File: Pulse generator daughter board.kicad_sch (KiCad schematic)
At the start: 27 parts, among them J1 PWM1 input, J2 PWM2 input, J3 Vin1, J4 Vin1_GND, J5 Vin2, J6 Vin2_GND, U1 TC4427, U2 TC4427

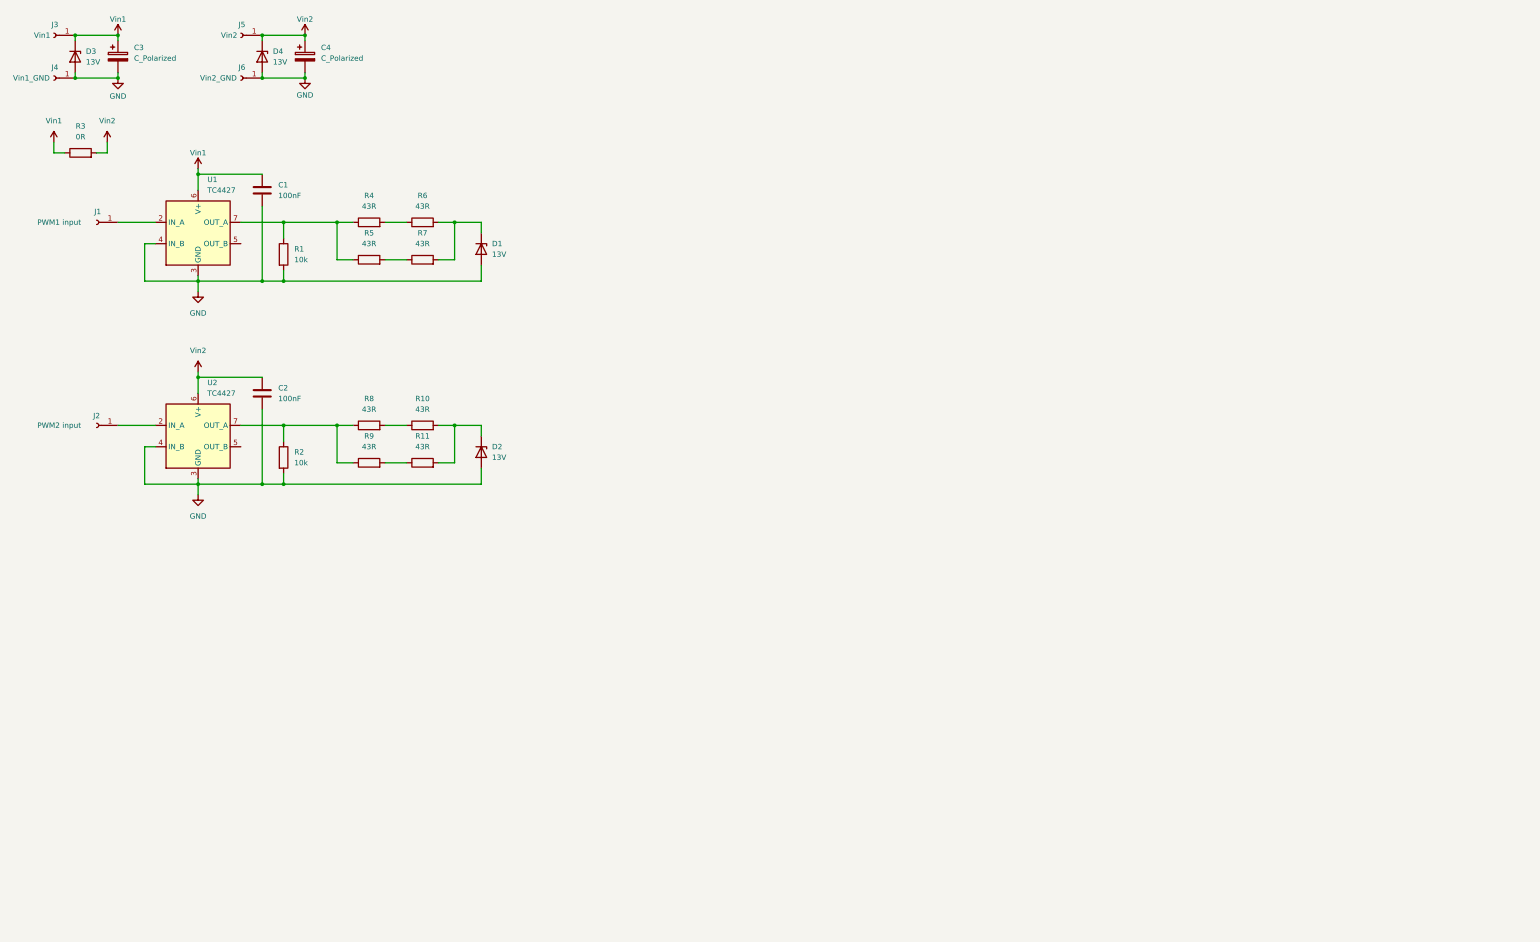
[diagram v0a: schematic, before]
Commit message: PWMs and DWMs done
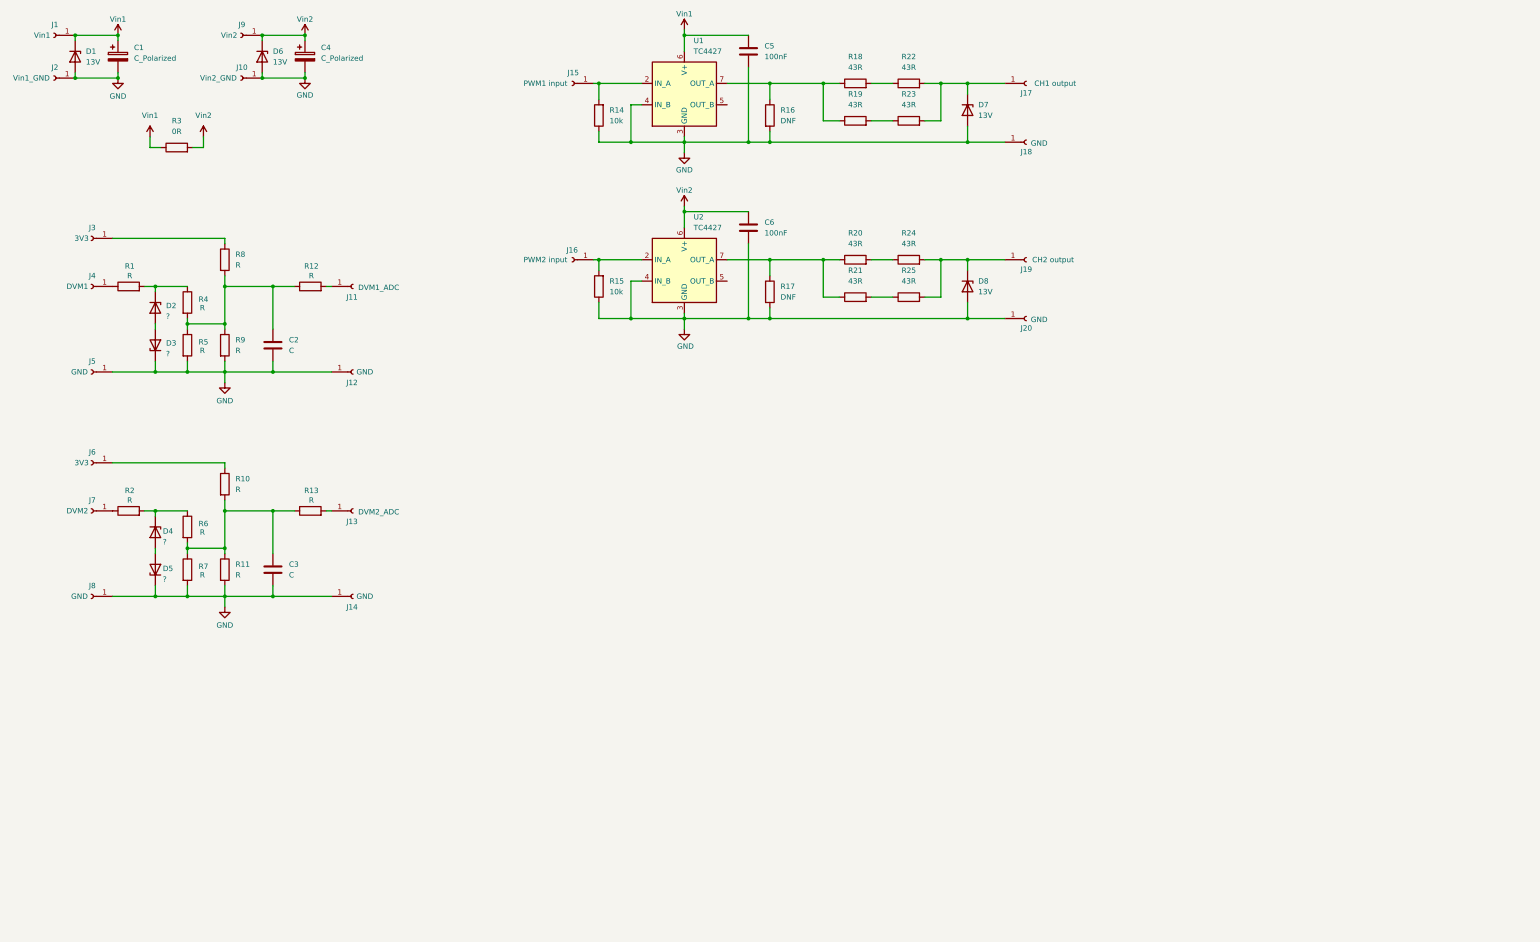
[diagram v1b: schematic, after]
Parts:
- added C2, C3: C, symbol Device:C
- added D2, D3, D4, D5: ?, symbol Device:D_Zener
- added J11: DVM1_ADC, symbol Connector:Conn_01x01_Socket
- added J12, J14, J18, J20, J5, J8: GND, symbol Connector:Conn_01x01_Socket
- added J13: DVM2_ADC, symbol Connector:Conn_01x01_Socket
- added J17: CH1 output, symbol Connector:Conn_01x01_Socket
- added J19: CH2 output, symbol Connector:Conn_01x01_Socket
- added J3, J6: 3V3, symbol Connector:Conn_01x01_Socket
- added J4: DVM1, symbol Connector:Conn_01x01_Socket
- added J7: DVM2, symbol Connector:Conn_01x01_Socket
- added R1, R10, R11, R12, R13, R2, R4, R5, R6, R7, R8, R9: R, symbol Device:R
- added R14, R15: 10k, symbol Device:R
- R16: renamed from R1; value 10k -> DNF
- R17: renamed from R2; value 10k -> DNF
- renumbered C3 to C1, C1 to C5, C2 to C6, D3 to D1, D4 to D6, D1 to D7, D2 to D8, J3 to J1, J6 to J10, J1 to J15, J2 to J16, J4 to J2, J5 to J9, R4 to R18, R5 to R19, R8 to R20, R9 to R21, R6 to R22, R7 to R23, R10 to R24, R11 to R25
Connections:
- net GND: now also C2.2, C3.2, D3.1 (K), D5.1 (K), J12.1 (Pin_1), J14.1 (Pin_1), J18.1 (Pin_1), J20.1 (Pin_1), J5.1 (Pin_1), J8.1 (Pin_1), R11.2, R14.1, R15.1, R5.2, R7.2, R9.2
- net at J15.1 (Pin_1), U1.2 (IN_A): now also R14.2
- net at D7.1 (K), R22.2, R23.2: now also J17.1 (Pin_1)
- net at D8.1 (K), R24.2, R25.2: now also J19.1 (Pin_1)
- net at J16.1 (Pin_1), U2.2 (IN_A): now also R15.2
- new net: D2.1 (K), R1.2, R4.1
- new net: D2.2 (A), D3.2 (A)
- new net: J6.1 (Pin_1), R10.1
- new net: J13.1 (Pin_1), R13.2
- new net: C3.1, R10.2, R11.1, R13.1, R6.2, R7.1
- new net: J3.1 (Pin_1), R8.1
- new net: C2.1, R12.1, R4.2, R5.1, R8.2, R9.1
- new net: J4.1 (Pin_1), R1.1
- new net: J7.1 (Pin_1), R2.1
- new net: J11.1 (Pin_1), R12.2
- new net: D4.1 (K), R2.2, R6.1
- new net: D4.2 (A), D5.2 (A)
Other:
- moved on the sheet: C5, C6, D7, D8, J15, J16, R16, R17, R18, R19, R20, R21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

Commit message: Progress 2 on schematic and PCB
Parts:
- removed J11: DVM1_ADC, symbol Connector:Conn_01x01_Socket
- removed J13: DVM2_ADC, symbol Connector:Conn_01x01_Socket
- removed J15: PWM1 input, symbol Connector:Conn_01x01_Socket
- removed J16: PWM2 input, symbol Connector:Conn_01x01_Socket
- added C1: 10nF, symbol Device:C
- added C4, C5, C9: C, symbol Device:C
- added C6: 100nF, symbol Device:C
- added J15: CN8, Connector_PinHeader_2.54mm:PinHeader_2x08_P2.54mm_Vertical, symbol Connector_Generic:Conn_02x08_Odd_Even
- added J16: CN9, Connector_PinHeader_2.54mm:PinHeader_2x15_P2.54mm_Vertical, symbol Connector_Generic:Conn_02x15_Odd_Even
- added J17: CN7, Connector_PinHeader_2.54mm:PinHeader_2x10_P2.54mm_Vertical, symbol Connector_Generic:Conn_02x10_Odd_Even
- added J18: CN10, Connector_PinHeader_2.54mm:PinHeader_2x17_P2.54mm_Vertical, symbol Connector_Generic:Conn_02x17_Odd_Even
- added U1: MAX31855KASA, Package_SO:SOIC-8_3.9x4.9mm_P1.27mm, symbol Sensor_Temperature:MAX31855KASA
- added U2: ADUM1402, Package_SO:SOIC-16W_7.5x10.3mm_P1.27mm, symbol Rafal_Library:ADUM1402
- C3: value C -> 100nF
- D1, D6, D7, D8: footprint (none) -> Diode_SMD:D_SMA_Handsoldering
- J12: value GND -> T-
- J14: value GND -> T+
- J7: value DVM2 -> DVM1
- R10, R11, R12, R13, R14, R15, R16, R17, R3, R4, R5, R6, R7, R8, R9: footprint (none) -> Resistor_SMD:R_0805_2012Metric_Pad1.20x1.40mm_HandSolder
- R18, R19, R20, R21, R22, R23, R24, R25: footprint (none) -> Resistor_SMD:R_2512_6332Metric_Pad1.40x3.35mm_HandSolder
- renumbered C5 to C10, C6 to C11, C1 to C2, C4 to C7, C2 to C8, J17 to J21, J18 to J22, J19 to J23, J20 to J24, U1 to U3, U2 to U4
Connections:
- net GND: now also R16.1, R17.1, C4.2, C5.2, C9.2, U2. (We2); no longer C3.2, J12.1 (Pin_1), J14.1 (Pin_1), R11.2, R16.2, R17.2, R9.2
- net Vin1: now also D6.1 (K); no longer D1.1 (K)
- net Vin2: now also D8.1 (K); no longer D6.1 (K)
- net at J6.1 (Pin_1), R10.1: now also C5.1
- net PWM1 _CH1: now reaches R14.2, U3.2 (IN_A)
- net PWM1 _CH1: now also J17.10 (Pin_10)
- net ADC2: now reaches R13.2
- net ADC2: now also C9.1, J16.19 (Pin_19)
- net at R10.2, R11.1, R13.1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: no longer C3.1
- net at D7.1 (K), J21.1 (Pin_1): now also R19.2, R21.2; no longer R22.2, R23.2
- net at R25.1: now also R23.2; no longer R21.2
- net at J23.1 (Pin_1), R24.2, R25.2: now also D1.1 (K); no longer D8.1 (K)
- net PWM1 _CH2: now reaches R15.2, U4.2 (IN_A)
- net PWM1 _CH2: now also J18.29 (Pin_29)
- net at R18.1, U3.7 (OUT_A): now also R16.2, R20.1; no longer R16.1, R19.1
- net at J3.1 (Pin_1), R8.1: now also C4.1
- net at R12.1, R4.2, R5.1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: no longer C8.1
- net at R18.2: now also R19.1; no longer R22.1
- net at R24.1: now also R22.2; no longer R20.2
- net at R23.1: now also R17.2, R22.1, U4.7 (OUT_A); no longer R19.2
- net ADC1: now reaches R12.2
- net ADC1: now also C8.1, J16.3 (Pin_3)
- new net: J17.15 (Pin_15), U2. (We2)
- new net: J17.19 (Pin_19), U2. (We2)
- new net: J17.2 (Pin_2), U2. (We2)
- new net: C1.1, J14.1 (Pin_1), U1.3 (T+)
- new net: C1.2, J12.1 (Pin_1), U1.2 (T-)
- new net: R20.2, R21.1
- new net: U1.5 (SCK), U2. (We2)
- new net: U1.6 (~{CS}), U2. (We2)
- new net: U1.7 (SO), U2. (We2)
- new net +3V3: U2. (We2)
- new net +3V3_TC: C3.1, C6.1, U1.4 (V_CC), U2. (We2)
- new net OV_TC: C3.2, C6.2, U1.1 (GND), U2. (We2)
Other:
- moved on the sheet: C10, C11, C2, C7, C8, D2, D3, D7, J1, J10, J2, J21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

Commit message: Progress on PCB 29.11.2024
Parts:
- removed C2, C7: C_Polarized, symbol Device:C_Polarized
- removed D5: ?, symbol Device:D_Zener
- removed J5, J8: GND, symbol Connector:Conn_01x01_Socket
- added C1, C2, C4, C6, C9: C, Capacitor_SMD:C_0805_2012Metric_Pad1.18x1.45mm_HandSolder, symbol Device:C
- added C13: 100nF, Capacitor_SMD:C_0805_2012Metric_Pad1.18x1.45mm_HandSolder, symbol Device:C
- added D9: 20V, Diode_SMD:D_SOD-323F, symbol Device:D_Zener
- added U1: RYK-053.3SH, Rafal:RYK-053.3SH, symbol Rafal_Library:RYK-053.3S/H
- C10: renamed from C8; footprint (none) -> Capacitor_SMD:C_0805_2012Metric_Pad1.18x1.45mm_HandSolder
- C11: renamed from C9; footprint (none) -> Capacitor_SMD:C_0805_2012Metric_Pad1.18x1.45mm_HandSolder
- C12: renamed from C6; footprint (none) -> Capacitor_SMD:C_0805_2012Metric_Pad1.18x1.45mm_HandSolder
- C14: renamed from C10; footprint (none) -> Capacitor_SMD:C_0805_2012Metric_Pad1.18x1.45mm_HandSolder
- C15: renamed from C11; footprint (none) -> Capacitor_SMD:C_0805_2012Metric_Pad1.18x1.45mm_HandSolder
- C3: renamed from C1; footprint (none) -> Capacitor_SMD:C_0805_2012Metric_Pad1.18x1.45mm_HandSolder
- C5: renamed from C3; footprint (none) -> Capacitor_SMD:C_0805_2012Metric_Pad1.18x1.45mm_HandSolder
- C7: renamed from C4; footprint (none) -> Capacitor_SMD:C_0805_2012Metric_Pad1.18x1.45mm_HandSolder
- C8: renamed from C5; footprint (none) -> Capacitor_SMD:C_0805_2012Metric_Pad1.18x1.45mm_HandSolder
- D2, D3, D4: value ? -> 20V; footprint (none) -> Diode_SMD:D_SOD-323F
- J1, J10, J2, J9: footprint (none) -> Connector_Wire:SolderWire-0.5sqmm_1x01_D0.9mm_OD2.1mm
- J15: renamed from J21; footprint (none) -> Connector_Wire:SolderWire-0.5sqmm_1x01_D0.9mm_OD2.1mm
- J16: renamed from J22; footprint (none) -> Connector_Wire:SolderWire-0.5sqmm_1x01_D0.9mm_OD2.1mm
- J17: renamed from J23; footprint (none) -> Connector_Wire:SolderWire-0.5sqmm_1x01_D0.9mm_OD2.1mm
- J18: renamed from J24; footprint (none) -> Connector_Wire:SolderWire-0.5sqmm_1x01_D0.9mm_OD2.1mm
- J7: renamed from J14; footprint (none) -> Connector_Wire:SolderWire-0.5sqmm_1x01_D0.9mm_OD2.1mm
- J8: renamed from J12; footprint (none) -> Connector_Wire:SolderWire-0.5sqmm_1x01_D0.9mm_OD2.1mm
- renumbered D6 to D1, D8 to D6, D1 to D8, J15 to J11, J16 to J12, J17 to J13, J18 to J14, J6 to J5, J7 to J6, R20 to R19, R22 to R20, R23 to R21, R19 to R22, R21 to R23, U1 to U2, U2 to U3, U3 to U4, U4 to U5
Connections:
- net +3V3: now also U3.16 (Vdd2), C13.1; no longer U3. (We2)
- net GND: now also D4.1 (K), R11.2, R9.2, U3.10 (We2), U3.15 (GND2), U3.9 (GND2), C1.2, C13.2, C2.2, C9.2, D9.1 (K), U1.2 (-Vin); no longer D3.1 (K), U3. (We2)
- net OV_TC: now also U3.2 (GND1), U3.4 (Vib), U3.7 (We1), U3.8 (GND1), C4.2, C6.2, U1.5 (-Vout); no longer U3. (We2)
- net Vin1: now also C2.1
- net Vin2: now also C9.1
- net at D2.2 (A): now also D9.2 (A); no longer D3.2 (A)
- net at J13.15 (Pin_15): now also U3.11 (Vid); no longer U3. (We2)
- net at J13.19 (Pin_19): now also U3.14 (Voa); no longer U3. (We2)
- net at J13.2 (Pin_2): now also U3.12 (Vic); no longer U3. (We2)
- net at D4.2 (A): now also D3.2 (A)
- net at R2.2, R6.1: now also D3.1 (K); no longer D4.1 (K)
- net +5V: now reaches J11.9 (Pin_9)
- net +5V: now also C1.1, U1.1 (+Vin)
- net at U2.5 (SCK): now also U3.6 (Vod); no longer U3. (We2)
- net at U2.6 (~{CS}): now also U3.5 (Voc); no longer U3. (We2)
- net at U2.7 (SO): now also U3.3 (Via); no longer U3. (We2)
- net +3V3_TC: no longer names the net of C12.1, C5.1, U2.4 (V_CC)
- net +3V3_TC: now also U3.1 (Vdd1), C4.1, C6.1, U1.7 (+Vout); no longer U3. (We2)
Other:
- moved on the sheet: C11, C12, C3, C5, C8, J5, J6, J7, J8, R10, R11, R13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
